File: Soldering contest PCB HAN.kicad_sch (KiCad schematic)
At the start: 13 parts, among them J1 Screw_Terminal_01x02, Q1 2N3904, Q2 2N3904

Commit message: improved wiring and connected everything
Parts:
- removed BT1: BATTERY-6.8MM_SMD, Battery:BatteryHolder_Keystone_3002_1x2032, symbol SparkFun-Batteries:BATTERY-6.8MM_SMD
- added BT1: Battery_Cell, Battery:BatteryHolder_Keystone_3002_1x2032, symbol Device:Battery_Cell
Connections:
- net GND: now also BT1.2 (-)
- net at S1.1 (O): now also BT1.1 (+)
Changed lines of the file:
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@@
     (stroke (width 0) (type default) (color 0 0 0 0))
   )
-  (wire (pts (xy 71.755 74.93) (xy 71.755 90.17))
+  (wire (pts (xy 71.755 72.39) (xy 71.755 90.17))
     (stroke (width 0) (type default) (color 0 0 0 0))
   )
@@
     (pin "2")
   )
-  (symbol (lib_id "SparkFun-Batteries:BATTERY-6.8MM_SMD") (at 71.755 69.85 270) (unit 1)
-    (in_bom yes) (on_board yes)
-    (property "Reference" "BT1" (id 0) (at 73.025 66.675 90)
-      (effects (font (size 1.143 1.143)) (justify left))
-    )
-    (property "Value" "BATTERY-6.8MM_SMD" (id 1) (at 76.835 69.85 90)
-      (effects (font (size 1.143 1.143)) (justify left) hide)
-    )
-    (property "Footprint" "Battery:BatteryHolder_Keystone_3002_1x2032" (id 2) (at 78.105 69.85 0)
-      (effects (font (size 0.508 0.508)) hide)
-    )
-    (property "Datasheet" "" (id 3) (at 71.755 69.85 0)
-      (effects (font (size 1.27 1.27)) hide)
-    )
-    (property "Field4" "BATT-13734" (id 4) (at 76.835 73.025 90)
-      (effects (font (size 1.524 1.524)) (justify left) hide)
-    )
-    (property "Purpose" "C2032" (id 5) (at 85.725 68.58 90)
-      (effects (font (size 1.27 1.27)) hide)
-    )
-    (pin "+")
-    (pin "-")
-  )
   (symbol (lib_id "Device:C_Polarized") (at 83.82 73.025 90) (unit 1)
     (in_bom yes) (on_board yes)
@@
     (pin "1")
   )
+  (symbol (lib_id "Device:Battery_Cell") (at 71.755 69.85 0) (unit 1)
+    (in_bom yes) (on_board yes)
+    (property "Reference" "BT1" (id 0) (at 72.39 71.12 0)
+      (effects (font (size 1.27 1.27)) (justify left))
+    )
+    (property "Value" "Battery_Cell" (id 1) (at 74.93 69.0879 0)
+      (effects (font (size 1.27 1.27)) (justify left) hide)
+    )
+    (property "Footprint" "Battery:BatteryHolder_Keystone_3002_1x2032" (id 2) (at 71.755 68.326 90)
+      (effects (font (size 1.27 1.27)) hide)
+    )
+    (property "Datasheet" "~" (id 3) (at 71.755 68.326 90)
+      (effects (font (size 1.27 1.27)) hide)
+    )
+    (pin "1")
+    (pin "2")
+  )
   (sheet_instances
     (path "/" (page "1"))
@@
       (reference "#PWR01") (unit 1) (value "GND") (footprint "")
     )
-    (path "/44a5ce8e-2c11-4619-8ce9-b752075d2088"
-      (reference "BT1") (unit 1) (value "BATTERY-6.8MM_SMD") (footprint "Battery:BatteryHolder_Keystone_3002_1x2032")
+    (path "/ff5ddebd-fa0b-425a-8582-07d48577659b"
+      (reference "BT1") (unit 1) (value "Battery_Cell") (footprint "Battery:BatteryHolder_Keystone_3002_1x2032")
     )
     (path "/5c87c882-b6f1-48af-94eb-8b3a9c0bcf0b"

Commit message: archived 3d models
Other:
- moved on the sheet: BT1, C1, C2, D1, D2, J1, Q1, Q2, R1, R2, R3, R4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

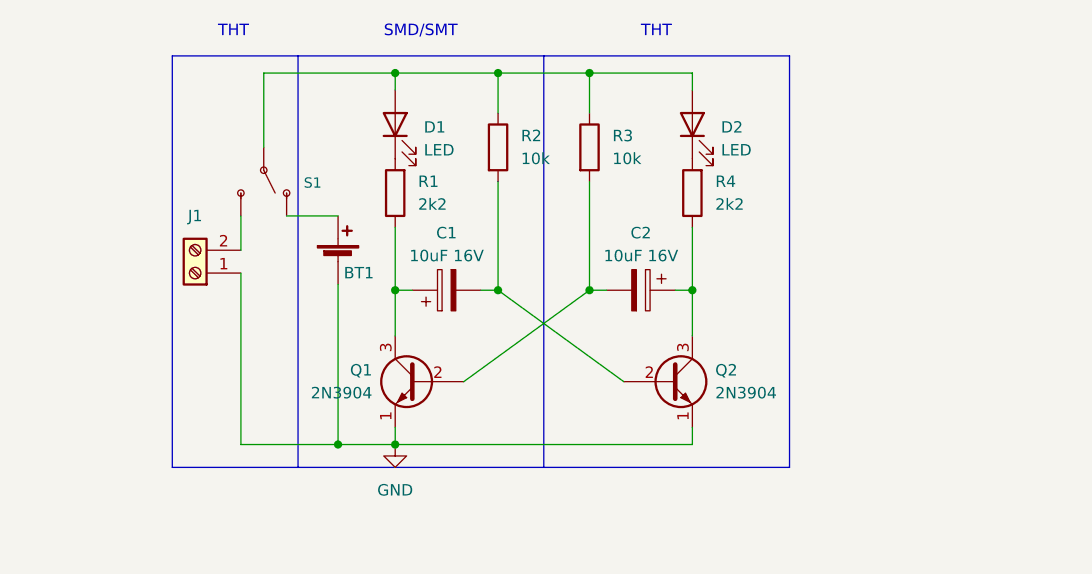
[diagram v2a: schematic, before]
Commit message: Finished V0.2
-added Remko's feedback
-changed a few component names to their smd parts
-added gitlab repo link to pcb (not yet uploaded to gitlab)
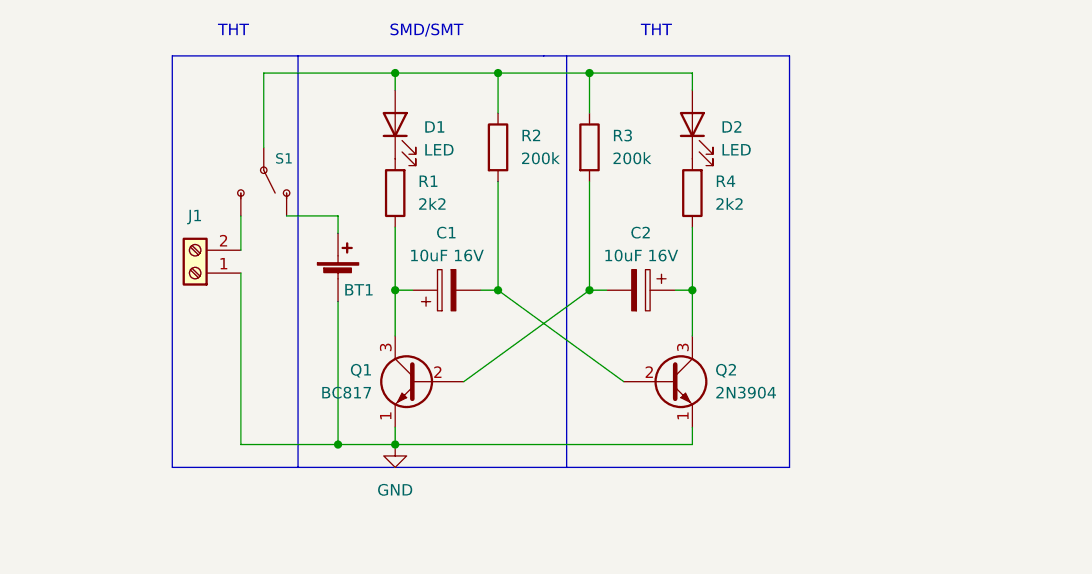
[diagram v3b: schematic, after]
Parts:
- Q1: value 2N3904 -> BC817
- R2, R3: value 10k -> 200k
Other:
- moved on the sheet: BT1
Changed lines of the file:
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@@
-    (stroke (width 0) (type default) (color 0 0 0 0))
-  )
-  (wire (pts (xy 88.9 69.85) (xy 88.9 87.63))
     (stroke (width 0) (type default) (color 0 0 0 0))
   )
@@
     (stroke (width 0) (type default) (color 0 0 0 0))
   )
-  (polyline (pts (xy 111.76 90.17) (xy 111.76 44.45))
+  (polyline (pts (xy 114.3 90.17) (xy 114.3 44.45))
     (stroke (width 0) (type default) (color 0 0 0 0))
   )
@@
     (stroke (width 0) (type default) (color 0 0 0 0))
   )
+  (wire (pts (xy 88.9 62.23) (xy 88.9 64.135))
+    (stroke (width 0) (type default) (color 0 0 0 0))
+  )
   (polyline (pts (xy 70.485 44.45) (xy 70.485 90.17))
     (stroke (width 0) (type default) (color 0 0 0 0))
@@
     (stroke (width 0) (type default) (color 0 0 0 0))
   )
+  (wire (pts (xy 88.9 71.755) (xy 88.9 87.63))
+    (stroke (width 0) (type default) (color 0 0 0 0))
+  )
   (wire (pts (xy 116.84 58.42) (xy 116.84 70.485))
     (stroke (width 0) (type default) (color 0 0 0 0))
   )
-  (text "SMD/SMT \n" (at 93.98 42.545 0)
+  (text "SMD/SMT \n" (at 94.615 42.545 0)
     (effects (font (size 1.27 1.27)) (justify left bottom))
   )
@@
       (effects (font (size 1.27 1.27)) (justify left))
     )
-    (property "Value" "10k" (id 1) (at 109.22 55.8799 0)
+    (property "Value" "200k" (id 1) (at 109.22 55.8799 0)
       (effects (font (size 1.27 1.27)) (justify left))
     )
@@
       (effects (font (size 1.27 1.27)) (justify left))
     )
-    (property "Value" "10k" (id 1) (at 119.38 55.8799 0)
+    (property "Value" "200k" (id 1) (at 119.38 55.8799 0)
       (effects (font (size 1.27 1.27)) (justify left))
     )
@@
   )
   (symbol (lib_id "SparkFun-Switches:SWITCH-SPDT-PTH-11.6X4.0MM-KIT") (at 80.645 57.15 270) (unit 1)
-    (in_bom yes) (on_board yes) (fields_autoplaced)
-    (property "Reference" "S1" (id 0) (at 85.09 58.5597 90)
+    (in_bom yes) (on_board yes)
+    (property "Reference" "S1" (id 0) (at 81.915 55.88 90)
       (effects (font (size 1.143 1.143)) (justify left))
     )
@@
       (effects (font (size 1.27 1.27)) (justify left))
     )
-    (property "Value" "2N3904" (id 1) (at 92.71 81.9149 0)
+    (property "Value" "BC817" (id 1) (at 92.71 81.9149 0)
       (effects (font (size 1.27 1.27)) (justify left))
     )
@@
       (effects (font (size 1.27 1.27) italic) (justify left) hide)
     )
-    (property "Datasheet" "https://www.onsemi.com/pub/Collateral/2N3903-D.PDF" (id 3) (at 97.79 80.645 0)
+    (property "Datasheet" "https://assets.nexperia.com/documents/data-sheet/BC817_SER.pdf" (id 3) (at 97.79 80.645 0)
       (effects (font (size 1.27 1.27)) (justify left) hide)
     )
@@
     (pin "1")
   )
-  (symbol (lib_id "Device:Battery_Cell") (at 88.9 67.31 0) (unit 1)
+  (symbol (lib_id "Device:Battery_Cell") (at 88.9 69.215 0) (unit 1)
     (in_bom yes) (on_board yes)
-    (property "Reference" "BT1" (id 0) (at 89.535 68.58 0)
-      (effects (font (size 1.27 1.27)) (justify left))
-    )
-    (property "Value" "Battery_Cell" (id 1) (at 92.075 66.5479 0)
+    (property "Reference" "BT1" (id 0) (at 89.535 70.485 0)
+      (effects (font (size 1.27 1.27)) (justify left))
+    )
+    (property "Value" "Battery_Cell" (id 1) (at 92.075 68.4529 0)
       (effects (font (size 1.27 1.27)) (justify left) hide)
     )
-    (property "Footprint" "Battery:BatteryHolder_Keystone_3002_1x2032" (id 2) (at 88.9 65.786 90)
-      (effects (font (size 1.27 1.27)) hide)
-    )
-    (property "Datasheet" "~" (id 3) (at 88.9 65.786 90)
+    (property "Footprint" "Battery:BatteryHolder_Keystone_3002_1x2032" (id 2) (at 88.9 67.691 90)
+      (effects (font (size 1.27 1.27)) hide)
+    )
+    (property "Datasheet" "~" (id 3) (at 88.9 67.691 90)
       (effects (font (size 1.27 1.27)) hide)
     )
@@
     )
     (path "/6b424259-f8a0-4482-996c-adc9565aa863"
-      (reference "Q1") (unit 1) (value "2N3904") (footprint "Package_TO_SOT_SMD:SOT-23_Handsoldering")
+      (reference "Q1") (unit 1) (value "BC817") (footprint "Package_TO_SOT_SMD:SOT-23_Handsoldering")
     )
     (path "/0fd58cd3-0637-4e39-b339-0859c358a065"
@@
     )
     (path "/5eba335f-f9b7-4f96-8244-9f11f5b02fc1"
-      (reference "R2") (unit 1) (value "10k") (footprint "Resistor_SMD:R_0805_2012Metric_Pad1.20x1.40mm_HandSolder")
+      (reference "R2") (unit 1) (value "200k") (footprint "Resistor_SMD:R_0805_2012Metric_Pad1.20x1.40mm_HandSolder")
     )
     (path "/5fd75fa8-c971-4180-8d4d-419bf5fd463a"
-      (reference "R3") (unit 1) (value "10k") (footprint "Resistor_THT:R_Axial_DIN0204_L3.6mm_D1.6mm_P2.54mm_Vertical")
+      (reference "R3") (unit 1) (value "200k") (footprint "Resistor_THT:R_Axial_DIN0204_L3.6mm_D1.6mm_P2.54mm_Vertical")
     )
     (path "/22a04216-54cb-44fe-9b76-e181b36e1a9f"

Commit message: improved values
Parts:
- R1, R4: value 2k2 -> 400
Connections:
- net at D2.1 (K): now also C2.1, Q2.3 (C); no longer R4.2
- net at R2.1, R3.1, S1.2 (P): now also R1.2, R4.2; no longer D1.2 (A), D2.2 (A)
- net at C1.1, Q1.3 (C): now also D1.1 (K); no longer R1.1
- new net: D2.2 (A), R4.1
- new net: D1.2 (A), R1.1
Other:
- moved on the sheet: D1, D2, R1, R4
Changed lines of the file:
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@@
     (effects (font (size 1.27 1.27)) (justify left bottom))
   )
-  (symbol (lib_id "Device:LED") (at 128.27 52.07 90) (unit 1)
-    (in_bom yes) (on_board yes) (fields_autoplaced)
-    (property "Reference" "D2" (id 0) (at 131.445 52.3874 90)
-      (effects (font (size 1.27 1.27)) (justify right))
-    )
-    (property "Value" "LED" (id 1) (at 131.445 54.9274 90)
-      (effects (font (size 1.27 1.27)) (justify right))
-    )
-    (property "Footprint" "LED_THT:LED_D5.0mm_Clear" (id 2) (at 128.27 52.07 0)
-      (effects (font (size 1.27 1.27)) hide)
-    )
-    (property "Datasheet" "~" (id 3) (at 128.27 52.07 0)
+  (symbol (lib_id "Device:LED") (at 128.27 59.69 90) (unit 1)
+    (in_bom yes) (on_board yes)
+    (property "Reference" "D2" (id 0) (at 131.445 58.42 90)
+      (effects (font (size 1.27 1.27)) (justify right))
+    )
+    (property "Value" "LED" (id 1) (at 131.445 60.96 90)
+      (effects (font (size 1.27 1.27)) (justify right))
+    )
+    (property "Footprint" "LED_THT:LED_D5.0mm_Clear" (id 2) (at 128.27 59.69 0)
+      (effects (font (size 1.27 1.27)) hide)
+    )
+    (property "Datasheet" "~" (id 3) (at 128.27 59.69 0)
       (effects (font (size 1.27 1.27)) hide)
     )
@@
     (pin "2")
   )
-  (symbol (lib_id "Device:R") (at 128.27 59.69 180) (unit 1)
-    (in_bom yes) (on_board yes) (fields_autoplaced)
-    (property "Reference" "R4" (id 0) (at 130.81 58.4199 0)
-      (effects (font (size 1.27 1.27)) (justify right))
-    )
-    (property "Value" "2k2" (id 1) (at 130.81 60.9599 0)
-      (effects (font (size 1.27 1.27)) (justify right))
-    )
-    (property "Footprint" "Resistor_THT:R_Axial_DIN0207_L6.3mm_D2.5mm_P7.62mm_Horizontal" (id 2) (at 130.048 59.69 90)
-      (effects (font (size 1.27 1.27)) hide)
-    )
-    (property "Datasheet" "~" (id 3) (at 128.27 59.69 0)
+  (symbol (lib_id "Device:R") (at 128.27 52.07 180) (unit 1)
+    (in_bom yes) (on_board yes) (fields_autoplaced)
+    (property "Reference" "R4" (id 0) (at 130.81 50.7999 0)
+      (effects (font (size 1.27 1.27)) (justify right))
+    )
+    (property "Value" "400" (id 1) (at 130.81 53.3399 0)
+      (effects (font (size 1.27 1.27)) (justify right))
+    )
+    (property "Footprint" "Resistor_THT:R_Axial_DIN0207_L6.3mm_D2.5mm_P7.62mm_Horizontal" (id 2) (at 130.048 52.07 90)
+      (effects (font (size 1.27 1.27)) hide)
+    )
+    (property "Datasheet" "~" (id 3) (at 128.27 52.07 0)
       (effects (font (size 1.27 1.27)) hide)
     )
@@
     (pin "3")
   )
-  (symbol (lib_id "Device:LED") (at 95.25 52.07 90) (unit 1)
-    (in_bom yes) (on_board yes) (fields_autoplaced)
-    (property "Reference" "D1" (id 0) (at 98.425 52.3874 90)
-      (effects (font (size 1.27 1.27)) (justify right))
-    )
-    (property "Value" "LED" (id 1) (at 98.425 54.9274 90)
-      (effects (font (size 1.27 1.27)) (justify right))
-    )
-    (property "Footprint" "LED_SMD:LED_0805_2012Metric_Pad1.15x1.40mm_HandSolder" (id 2) (at 95.25 52.07 0)
+  (symbol (lib_id "Device:LED") (at 95.25 59.69 90) (unit 1)
+    (in_bom yes) (on_board yes)
+    (property "Reference" "D1" (id 0) (at 98.425 58.42 90)
+      (effects (font (size 1.27 1.27)) (justify right))
+    )
+    (property "Value" "LED" (id 1) (at 98.425 60.96 90)
+      (effects (font (size 1.27 1.27)) (justify right))
+    )
+    (property "Footprint" "LED_SMD:LED_0805_2012Metric_Pad1.15x1.40mm_HandSolder" (id 2) (at 95.25 59.69 0)
+      (effects (font (size 1.27 1.27)) hide)
+    )
+    (property "Datasheet" "~" (id 3) (at 95.25 59.69 0)
+      (effects (font (size 1.27 1.27)) hide)
+    )
+    (pin "1")
+    (pin "2")
+  )
+  (symbol (lib_id "Device:R") (at 95.25 52.07 180) (unit 1)
+    (in_bom yes) (on_board yes) (fields_autoplaced)
+    (property "Reference" "R1" (id 0) (at 97.79 50.7999 0)
+      (effects (font (size 1.27 1.27)) (justify right))
+    )
+    (property "Value" "400" (id 1) (at 97.79 53.3399 0)
+      (effects (font (size 1.27 1.27)) (justify right))
+    )
+    (property "Footprint" "Resistor_SMD:R_01005_0402Metric_Pad0.57x0.30mm_HandSolder" (id 2) (at 97.028 52.07 90)
       (effects (font (size 1.27 1.27)) hide)
     )
     (property "Datasheet" "~" (id 3) (at 95.25 52.07 0)
-      (effects (font (size 1.27 1.27)) hide)
-    )
-    (pin "1")
-    (pin "2")
-  )
-  (symbol (lib_id "Device:R") (at 95.25 59.69 180) (unit 1)
-    (in_bom yes) (on_board yes) (fields_autoplaced)
-    (property "Reference" "R1" (id 0) (at 97.79 58.4199 0)
-      (effects (font (size 1.27 1.27)) (justify right))
-    )
-    (property "Value" "2k2" (id 1) (at 97.79 60.9599 0)
-      (effects (font (size 1.27 1.27)) (justify right))
-    )
-    (property "Footprint" "Resistor_SMD:R_01005_0402Metric_Pad0.57x0.30mm_HandSolder" (id 2) (at 97.028 59.69 90)
-      (effects (font (size 1.27 1.27)) hide)
-    )
-    (property "Datasheet" "~" (id 3) (at 95.25 59.69 0)
       (effects (font (size 1.27 1.27)) hide)
     )
@@
     )
     (path "/d18fc897-0878-42f5-b8a2-449363703de6"
-      (reference "R1") (unit 1) (value "2k2") (footprint "Resistor_SMD:R_01005_0402Metric_Pad0.57x0.30mm_HandSolder")
+      (reference "R1") (unit 1) (value "400") (footprint "Resistor_SMD:R_01005_0402Metric_Pad0.57x0.30mm_HandSolder")
     )
     (path "/5eba335f-f9b7-4f96-8244-9f11f5b02fc1"
@@
     )
     (path "/22a04216-54cb-44fe-9b76-e181b36e1a9f"
-      (reference "R4") (unit 1) (value "2k2") (footprint "Resistor_THT:R_Axial_DIN0207_L6.3mm_D2.5mm_P7.62mm_Horizontal")
+      (reference "R4") (unit 1) (value "400") (footprint "Resistor_THT:R_Axial_DIN0207_L6.3mm_D2.5mm_P7.62mm_Horizontal")
     )
     (path "/6502d947-661b-4d45-91f3-16aac5eae88a"
